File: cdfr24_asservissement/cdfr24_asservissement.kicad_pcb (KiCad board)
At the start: 2 copper layers, 96.5 x 72.9 mm, 97 parts, among them J1 Connecteur batterie, J10 Conn_01x03, J11 Connecteur Odométrie, J12 Conn_01x03, J13 Conn_01x02, J14 Conn_01x02, J2 Conn_01x05, J3 Conn_01x03, J4 Conn_01x06_Pin, J5 Conn_ST_STDC14, J6 Conn_01x05, J7 Connecteur Programmation, J8 Conn_01x03, J9 Connecteur Odométrie, Q1 Q_NMOS_GDS, SW1 SW_DIP_x02, U1 LD1117S33TR_SOT223, U2 TVN 5-2411WI, U3 STM32F401RCTx

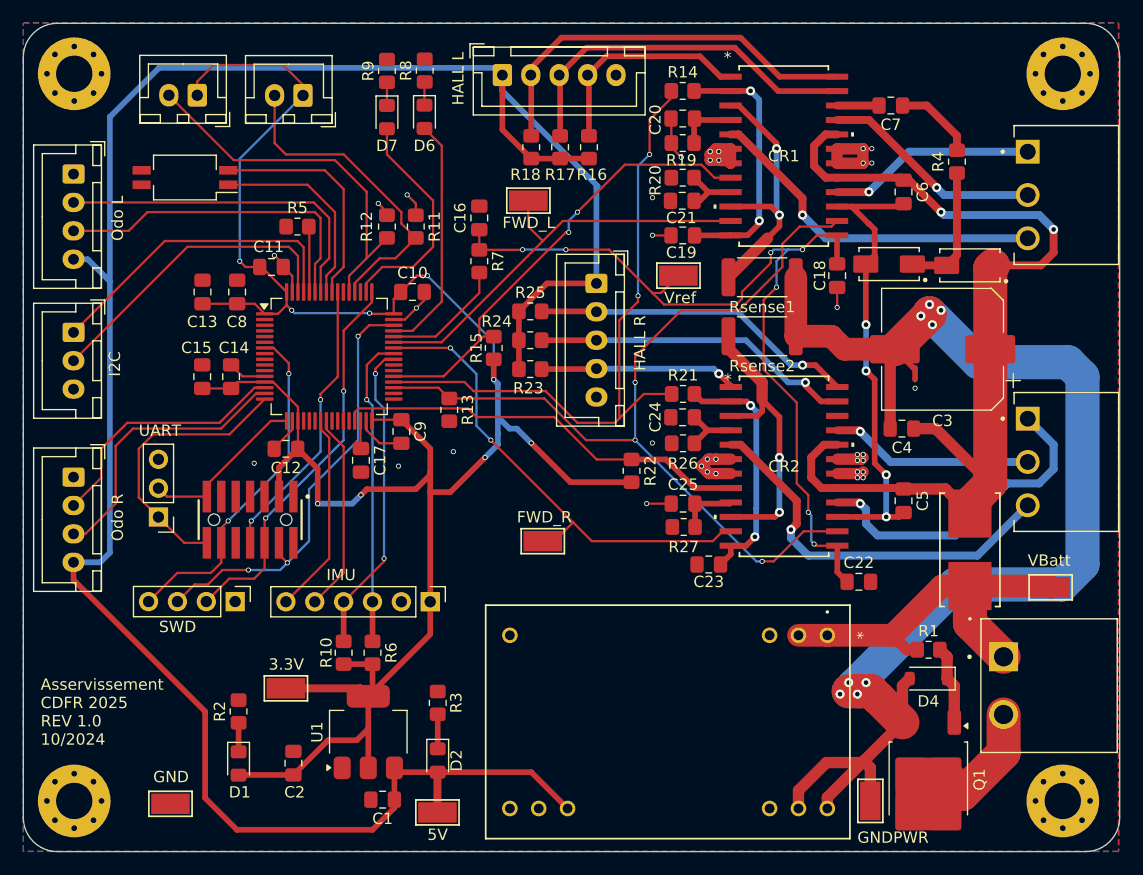
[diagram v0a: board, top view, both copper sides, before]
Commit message: Add text on PCB
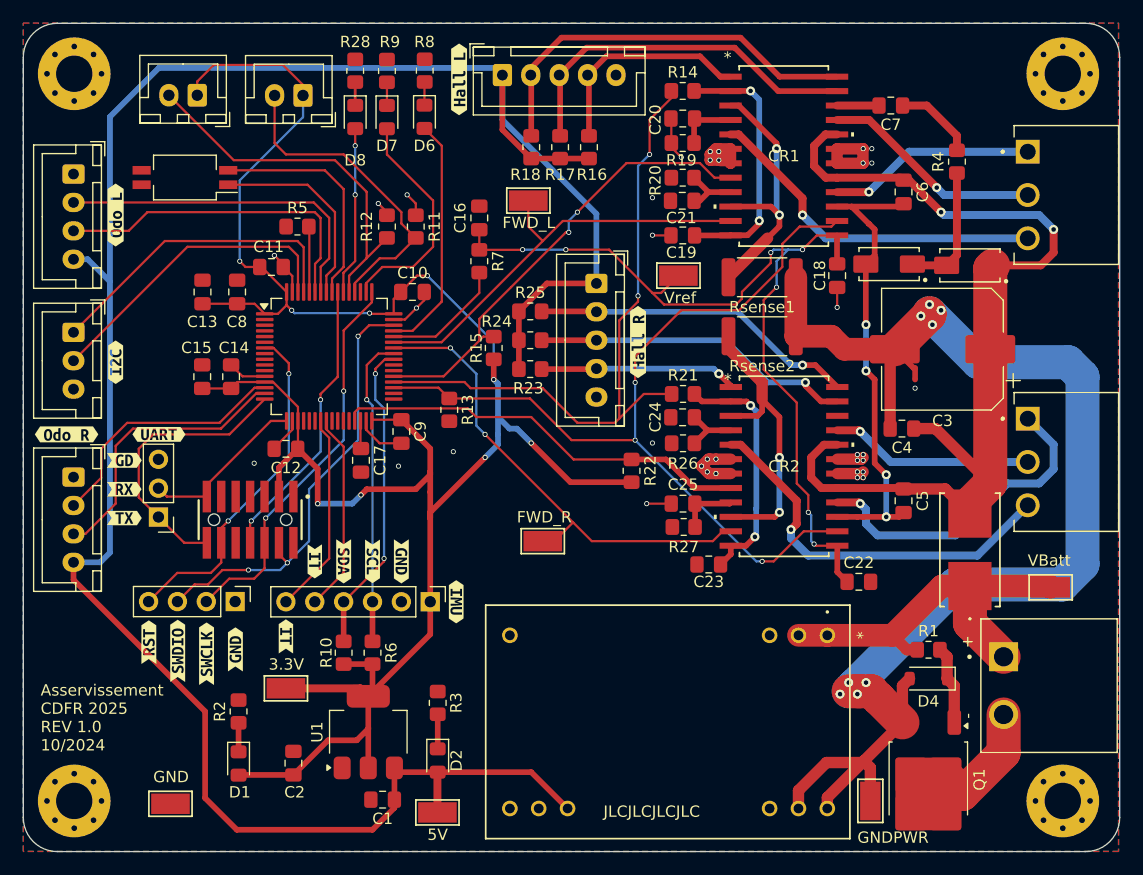
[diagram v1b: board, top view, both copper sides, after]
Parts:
- added D8: LED, LED_SMD:LED_0805_2012Metric_Pad1.15x1.40mm_HandSolder, F.Cu at (93.7, 34.8)
- added R28: 220, Resistor_SMD:R_0805_2012Metric_Pad1.20x1.40mm_HandSolder, F.Cu at (93.7, 30.7)
- added kibuzzard-670C1B62: G***, kibuzzard-670C1B62, F.Cu at (72.6, 43.4)
- added kibuzzard-670C1B77: G***, kibuzzard-670C1B77, F.Cu at (72.6, 56.4)
- added kibuzzard-670C1BB6: G***, kibuzzard-670C1BB6, F.Cu at (68.3, 62.7)
- added kibuzzard-670C1BE0: G***, kibuzzard-670C1BE0, F.Cu at (76.5, 62.7)
- added kibuzzard-670C1C38: G***, kibuzzard-670C1C38, F.Cu at (73.4, 67.6)
- added kibuzzard-670C1C44: G***, kibuzzard-670C1C44, F.Cu at (73.4, 70.1)
- added kibuzzard-670C1C88: G***, kibuzzard-670C1C88, F.Cu at (73.4, 65.0)
- added kibuzzard-670C1CA4: G***, kibuzzard-670C1CA4, F.Cu at (75.6, 81.0)
- added kibuzzard-670C1CC0: G***, kibuzzard-670C1CC0, F.Cu at (78.1, 81.8)
- added kibuzzard-670C1CCE: G***, kibuzzard-670C1CCE, F.Cu at (80.6, 82.0)
- added kibuzzard-670C1CDC: G***, kibuzzard-670C1CDC, F.Cu at (83.2, 81.7)
- added kibuzzard-670C1D0C: G***, kibuzzard-670C1D0C, F.Cu at (102.6, 77.5)
- added kibuzzard-670C1D22: G***, kibuzzard-670C1D22, F.Cu at (97.8, 73.9)
- added kibuzzard-670C1D36: G***, kibuzzard-670C1D36, F.Cu at (95.2, 73.9)
- added kibuzzard-670C1D6D: G***, kibuzzard-670C1D6D, F.Cu at (90.2, 73.9)
- added kibuzzard-670C1D87: G***, kibuzzard-670C1D87, F.Cu at (87.6, 80.5)
- added kibuzzard-670C1D91: G***, kibuzzard-670C1D91, F.Cu at (92.7, 73.9)
- added kibuzzard-670C1DC2: G***, kibuzzard-670C1DC2, F.Cu at (102.9, 31.5)
- added kibuzzard-670C1DD5: G***, kibuzzard-670C1DD5, F.Cu at (118.6, 54.6)
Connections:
- U3 pad 54: unconnected-(U3-PD2-Pad54) -> Net-(D8-A)
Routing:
- net Net-(D8-A): track 0.00 -> 14.8 mm, vias 0 -> 2
- net Net-(D8-K): track 0.00 -> 2.05 mm
- net +3.3V: track 198.3 -> 199.5 mm
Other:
- board text added: "+"
- board text added: "-"
- board text added: "JLCJLCJLCJLC"
- board text removed: "HALL L"
- board text removed: "HALL R"
- board text removed: "I2C"
- board text removed: "IMU"
- board text removed: "Odo L"
- board text removed: "Odo R"
- board text removed: "SWD"
- board text removed: "UART"
